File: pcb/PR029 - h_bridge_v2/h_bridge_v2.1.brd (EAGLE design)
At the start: 52.7 x 54.6 mm, 27 parts, among them IC1 L298

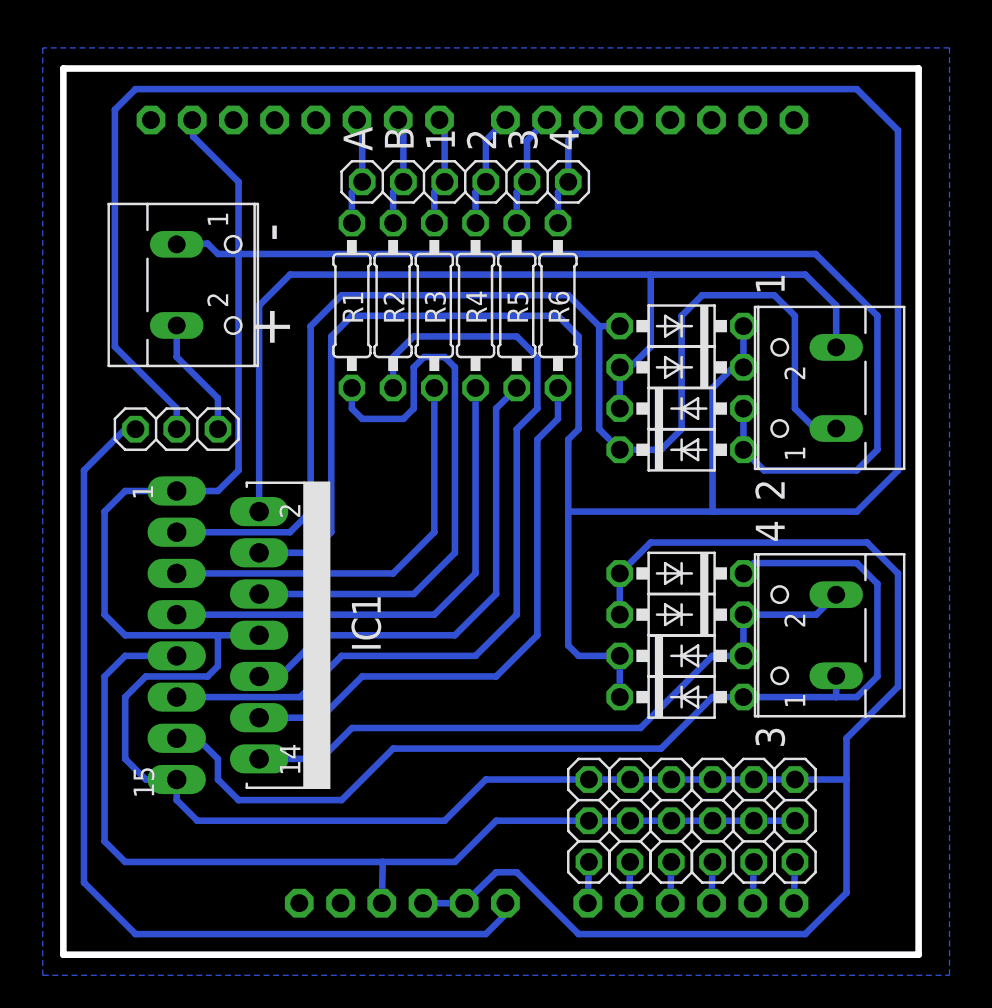
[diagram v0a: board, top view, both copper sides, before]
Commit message: 
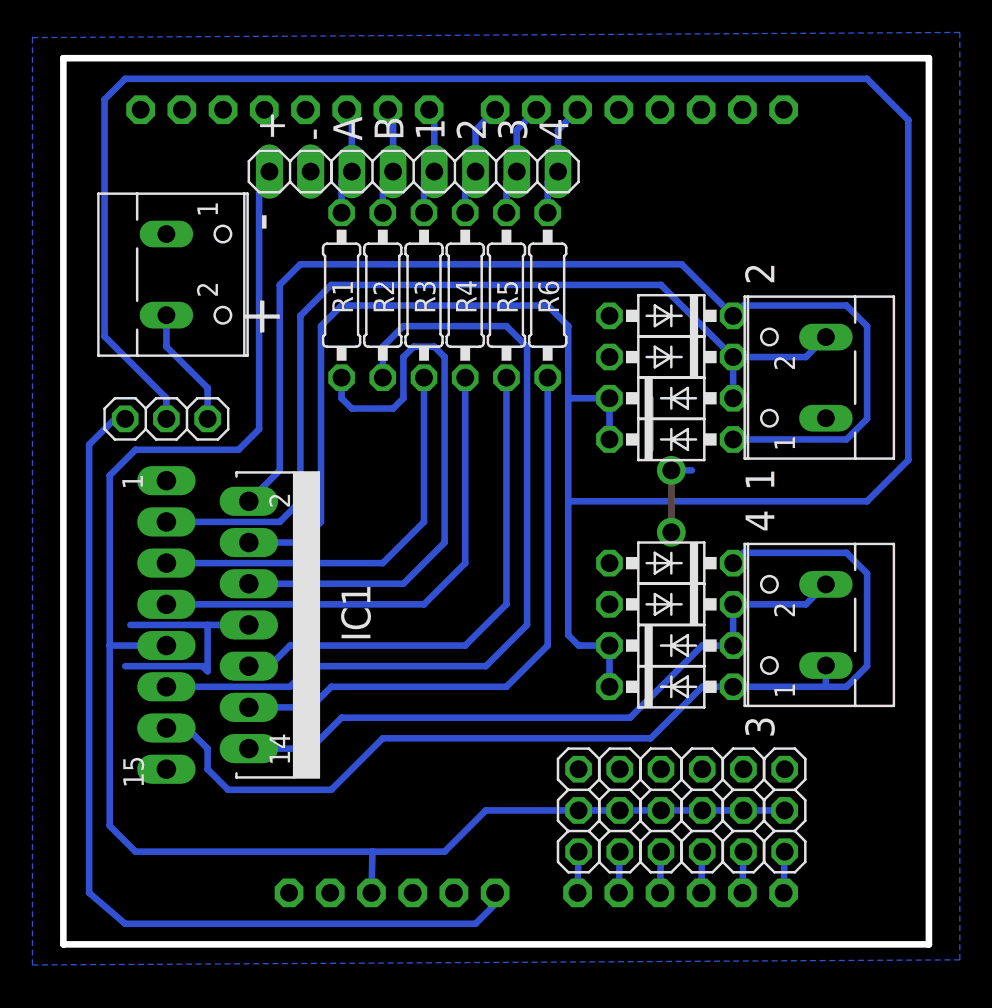
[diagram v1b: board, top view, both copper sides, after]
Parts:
- added JP9: (no value), h_bridge_v2:1X02
- moved D3 5.75 mm to (37.5, 36.8), turned to 180 degrees
- moved D4 5.75 mm to (37.5, 39.4), turned to 180 degrees
- moved D1 4.49 mm to (37.5, 34.3), turned to 0 degrees
- moved D2 4.49 mm to (37.5, 31.8), turned to 0 degrees
- moved JP2 0.90 mm to (6.35, 33.0)
- moved JP5 0.90 mm to (36.8, 8.89)
- moved JP6 0.90 mm to (39.4, 8.89)
- moved JP7 0.90 mm to (41.9, 8.89)
- moved X1 0.90 mm to (45.7, 35.6)
- moved IC1 0.90 mm to (14.0, 20.3)
- moved U$1 0.90 mm to (-2.60, 0.00)
- moved D5 0.90 mm to (37.5, 19.1)
- moved D6 0.90 mm to (37.5, 16.5)
- moved D7 0.90 mm to (37.5, 21.6)
- moved JP1 0.90 mm to (24.1, 48.3)
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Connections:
- net VIN_A renamed VIN
- net VIN_B renamed PWR
- net +5V: now also JP9.1
- net GND: now also JP9.2
- net OUT1: now also X1.1; no longer X1.2
- net OUT2: now also X1.2; no longer X1.1
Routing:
- net GND: track 246.7 -> 23.6 mm, vias 0 -> 2
- net +5V: track 61.8 -> 97.5 mm
- net OUT2: track 77.1 -> 58.3 mm
- net +12V: track 184.6 -> 178.1 mm
- net OUT1: track 61.8 -> 67.4 mm
- net N$6: track 35.0 -> 36.5 mm
- net N$5: track 29.9 -> 31.4 mm
- net N$2: track 51.3 -> 52.8 mm
- net VIN: track 58.1 -> 57.5 mm
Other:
- board size 52.7 x 54.6 mm -> 53.3 x 54.6 mm
- board text added: "PWR"
- board text removed: "POWER"

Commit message: 
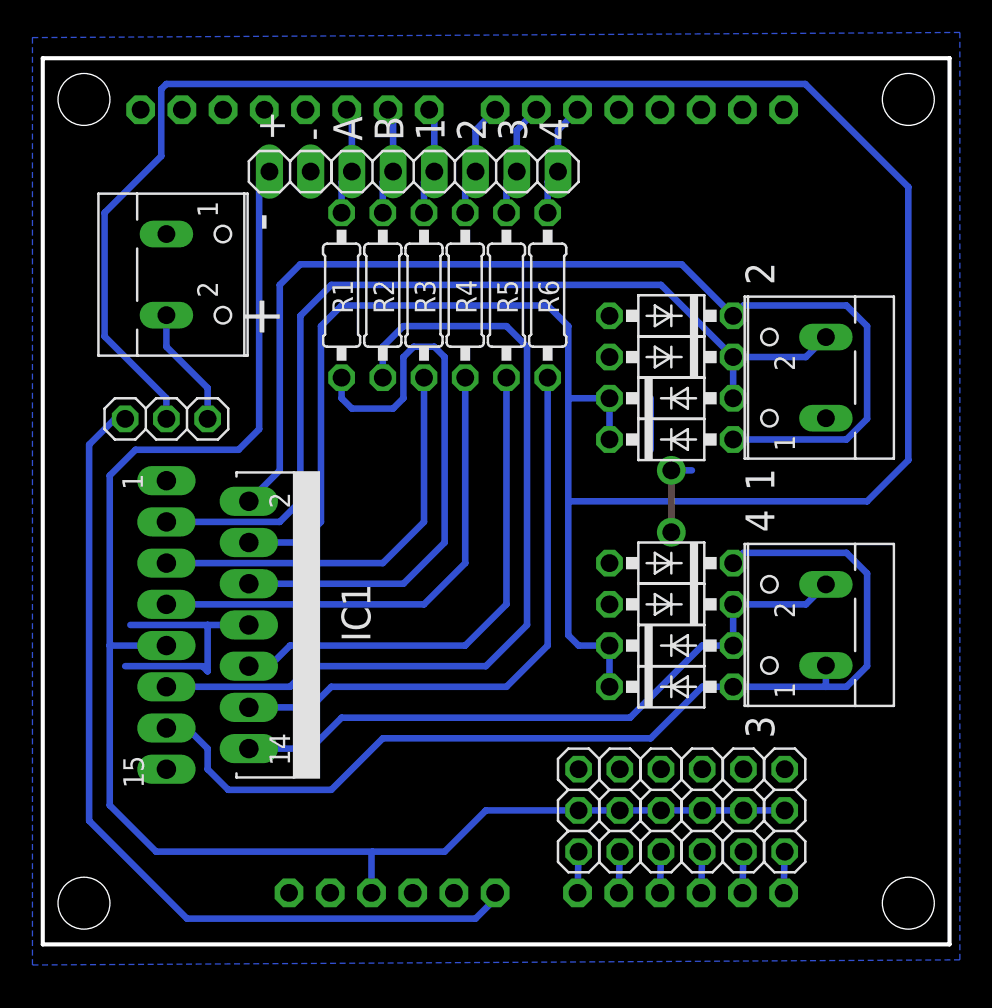
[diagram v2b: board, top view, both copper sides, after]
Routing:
- net +12V: track 178.1 -> 173.8 mm
- net VIN: track 57.5 -> 54.5 mm
- net +5V: track 97.5 -> 96.7 mm
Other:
- board size 53.3 x 54.6 mm -> 55.9 x 54.6 mm
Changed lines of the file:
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@@
 <layer number="43" name="vRestrict" color="2" fill="10" visible="yes" active="yes"/>
 <layer number="44" name="Drills" color="7" fill="1" visible="no" active="yes"/>
-<layer number="45" name="Holes" color="7" fill="1" visible="no" active="yes"/>
+<layer number="45" name="Holes" color="7" fill="1" visible="yes" active="yes"/>
 <layer number="46" name="Milling" color="3" fill="1" visible="no" active="yes"/>
 <layer number="47" name="Measures" color="7" fill="1" visible="no" active="yes"/>
@@
 <board>
 <plain>
-<wire x1="0" y1="0.635" x2="53.34" y2="0.635" width="0.4064" layer="20"/>
-<wire x1="53.34" y1="0.635" x2="53.34" y2="55.245" width="0.4064" layer="20"/>
-<wire x1="53.34" y1="55.245" x2="0" y2="55.245" width="0.4064" layer="20"/>
-<wire x1="0" y1="55.245" x2="0" y2="0.635" width="0.4064" layer="20"/>
+<wire x1="-1.27" y1="0.635" x2="54.61" y2="0.635" width="0.254" layer="20"/>
+<wire x1="54.61" y1="0.635" x2="54.61" y2="55.245" width="0.254" layer="20"/>
+<wire x1="54.61" y1="55.245" x2="-1.27" y2="55.245" width="0.254" layer="20"/>
+<wire x1="-1.27" y1="55.245" x2="-1.27" y2="0.635" width="0.254" layer="20"/>
 <text x="10.795" y="40.64" size="2.54" layer="25" font="vector" ratio="12" rot="R270">+</text>
 <text x="10.795" y="45.72" size="2.54" layer="25" font="vector" ratio="12" rot="R270">-</text>
@@
 <text x="13.6525" y="50.165" size="1.778" layer="25" font="vector" ratio="12" rot="R90">+</text>
 <text x="16.1925" y="50.165" size="1.778" layer="25" font="vector" ratio="12" rot="R90">-</text>
+<hole x="1.27" y="3.175" drill="3.2"/>
+<hole x="52.07" y="3.175" drill="3.2"/>
+<hole x="52.07" y="52.705" drill="3.2"/>
+<hole x="1.27" y="52.705" drill="3.2"/>
 </plain>
 <attributes>
@@
 <wire x1="31.115" y1="27.94" x2="49.53" y2="27.94" width="0.4064" layer="16"/>
 <wire x1="49.53" y1="27.94" x2="52.07" y2="30.48" width="0.4064" layer="16"/>
-<wire x1="52.07" y1="30.48" x2="52.07" y2="51.435" width="0.4064" layer="16"/>
-<wire x1="52.07" y1="51.435" x2="49.53" y2="53.975" width="0.4064" layer="16"/>
-<wire x1="49.53" y1="53.975" x2="3.81" y2="53.975" width="0.4064" layer="16"/>
-<wire x1="3.81" y1="53.975" x2="2.54" y2="52.705" width="0.4064" layer="16"/>
+<wire x1="52.07" y1="30.48" x2="52.07" y2="47.3075" width="0.4064" layer="16"/>
+<wire x1="52.07" y1="47.3075" x2="45.72" y2="53.6575" width="0.4064" layer="16"/>
+<wire x1="45.72" y1="53.6575" x2="6.35" y2="53.6575" width="0.4064" layer="16"/>
 <wire x1="11.43" y1="25.4" x2="14.605" y2="25.4" width="0.4064" layer="16"/>
 <wire x1="14.605" y1="25.4" x2="15.875" y2="26.67" width="0.4064" layer="16"/>
@@
 <wire x1="17.145" y1="40.005" x2="29.845" y2="40.005" width="0.4064" layer="16"/>
 <wire x1="29.845" y1="40.005" x2="31.115" y2="38.735" width="0.4064" layer="16"/>
-<wire x1="2.54" y1="52.705" x2="2.54" y2="38.1" width="0.4064" layer="16"/>
 <wire x1="2.54" y1="38.1" x2="6.35" y2="34.29" width="0.4064" layer="16"/>
 <wire x1="6.35" y1="34.29" x2="6.35" y2="33.02" width="0.4064" layer="16"/>
@@
 <wire x1="33.655" y1="31.75" x2="33.655" y2="34.29" width="0.4064" layer="16"/>
 <wire x1="33.655" y1="34.29" x2="31.115" y2="34.29" width="0.4064" layer="16"/>
+<wire x1="2.54" y1="38.1" x2="2.54" y2="45.72" width="0.4064" layer="16"/>
+<wire x1="2.54" y1="45.72" x2="6.0325" y2="49.2125" width="0.4064" layer="16"/>
+<wire x1="6.0325" y1="49.2125" x2="6.0325" y2="53.34" width="0.4064" layer="16"/>
+<wire x1="6.0325" y1="53.34" x2="6.35" y2="53.6575" width="0.4064" layer="16"/>
 </signal>
 <signal name="OUT1">
@@
 <contactref element="JP3" pad="2"/>
 <contactref element="JP8" pad="2"/>
-<wire x1="19.05" y1="6.35" x2="18.9865" y2="3.81" width="0.4064" layer="16"/>
-<wire x1="4.445" y1="6.35" x2="19.05" y2="6.35" width="0.4064" layer="16"/>
-<wire x1="2.8575" y1="7.9375" x2="4.445" y2="6.35" width="0.4064" layer="16"/>
+<wire x1="5.715" y1="6.35" x2="19.05" y2="6.35" width="0.4064" layer="16"/>
+<wire x1="19.05" y1="6.35" x2="23.495" y2="6.35" width="0.4064" layer="16"/>
+<wire x1="2.8575" y1="9.2075" x2="5.715" y2="6.35" width="0.4064" layer="16"/>
 <wire x1="2.8575" y1="19.05" x2="6.35" y2="19.05" width="0.4064" layer="16"/>
 <wire x1="41.91" y1="8.89" x2="44.45" y2="8.89" width="0.4064" layer="16"/>
@@
 <wire x1="26.035" y1="8.89" x2="31.75" y2="8.89" width="0.4064" layer="16"/>
 <wire x1="23.495" y1="6.35" x2="26.035" y2="8.89" width="0.4064" layer="16"/>
-<wire x1="19.05" y1="6.35" x2="23.495" y2="6.35" width="0.4064" layer="16"/>
 <contactref element="JP9" pad="1"/>
-<wire x1="2.8575" y1="7.9375" x2="2.8575" y2="19.05" width="0.4064" layer="16"/>
+<wire x1="2.8575" y1="9.2075" x2="2.8575" y2="19.05" width="0.4064" layer="16"/>
 <wire x1="12.7" y1="48.26" x2="12.065" y2="47.625" width="0.4064" layer="16"/>
 <wire x1="12.065" y1="47.625" x2="12.065" y2="32.385" width="0.4064" layer="16"/>
@@
 <wire x1="4.445" y1="31.115" x2="2.8575" y2="29.5275" width="0.4064" layer="16"/>
 <wire x1="2.8575" y1="29.5275" x2="2.8575" y2="19.05" width="0.4064" layer="16"/>
+<wire x1="18.9865" y1="3.81" x2="18.9865" y2="6.2865" width="0.4064" layer="16"/>
+<wire x1="18.9865" y1="6.2865" x2="19.05" y2="6.35" width="0.4064" layer="16"/>
 </signal>
 <signal name="PWR">
@@
 <contactref element="U$1" pad="VIN"/>
 <contactref element="JP2" pad="1"/>
-<wire x1="1.5875" y1="3.81" x2="3.81" y2="1.905" width="0.4064" layer="16"/>
-<wire x1="3.81" y1="1.905" x2="25.4" y2="1.905" width="0.4064" layer="16"/>
-<wire x1="1.5875" y1="3.81" x2="1.5875" y2="31.4325" width="0.4064" layer="16"/>
+<wire x1="1.5875" y1="8.255" x2="7.62" y2="2.2225" width="0.4064" layer="16"/>
+<wire x1="7.62" y1="2.2225" x2="25.4" y2="2.2225" width="0.4064" layer="16"/>
+<wire x1="1.5875" y1="8.255" x2="1.5875" y2="31.4325" width="0.4064" layer="16"/>
 <wire x1="1.5875" y1="31.4325" x2="3.175" y2="33.02" width="0.4064" layer="16"/>
 <wire x1="3.175" y1="33.02" x2="3.81" y2="33.02" width="0.4064" layer="16"/>
-<wire x1="25.4" y1="1.905" x2="26.67" y2="3.175" width="0.4064" layer="16"/>
-<wire x1="26.67" y1="3.175" x2="26.6065" y2="3.81" width="0.4064" layer="16"/>
+<wire x1="26.6065" y1="3.81" x2="26.6065" y2="3.429" width="0.4064" layer="16"/>
+<wire x1="26.6065" y1="3.429" x2="25.4" y2="2.2225" width="0.4064" layer="16"/>
 </signal>
 <signal name="N$16">
